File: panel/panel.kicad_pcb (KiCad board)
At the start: 0 parts

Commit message: LED matrix placement
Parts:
- added C1: 0.1uF, Capacitor_SMD:C_0603_1608Metric, F.Cu at (322.1, 98.3)
- added C2: 0.1uF, Capacitor_SMD:C_0603_1608Metric, F.Cu at (338.8, 87.2)
- added C3: 0.1uF, Capacitor_SMD:C_0603_1608Metric, F.Cu at (330.9, 93.8)
- added C4: 0.1uF, Capacitor_SMD:C_0603_1608Metric, F.Cu at (326.1, 98.3)
- added D1: LED_RABG, panel:MHPA1515RGBDT, F.Cu at (61.5, 61.5)
- added D10: LED_RABG, panel:MHPA1515RGBDT, F.Cu at (81.3, 61.5)
- added D100: LED_RABG, panel:MHPA1515RGBDT, F.Cu at (68.1, 74.7)
- added D101: LED_RABG, panel:MHPA1515RGBDT, F.Cu at (70.3, 74.7)
- added D102: LED_RABG, panel:MHPA1515RGBDT, F.Cu at (72.5, 74.7)
- added D103: LED_RABG, panel:MHPA1515RGBDT, F.Cu at (74.7, 74.7)
- added D104: LED_RABG, panel:MHPA1515RGBDT, F.Cu at (76.9, 74.7)
- added D105: LED_RABG, panel:MHPA1515RGBDT, F.Cu at (79.1, 74.7)
- added D106: LED_RABG, panel:MHPA1515RGBDT, F.Cu at (81.3, 74.7)
- added D107: LED_RABG, panel:MHPA1515RGBDT, F.Cu at (83.5, 74.7)
- added D108: LED_RABG, panel:MHPA1515RGBDT, F.Cu at (85.7, 74.7)
- added D109: LED_RABG, panel:MHPA1515RGBDT, F.Cu at (87.9, 74.7)
- added D11: LED_RABG, panel:MHPA1515RGBDT, F.Cu at (83.5, 61.5)
- added D110: LED_RABG, panel:MHPA1515RGBDT, F.Cu at (90.1, 74.7)
- added D111: LED_RABG, panel:MHPA1515RGBDT, F.Cu at (92.3, 74.7)
- added D112: LED_RABG, panel:MHPA1515RGBDT, F.Cu at (94.5, 74.7)
- added D113: LED_RABG, panel:MHPA1515RGBDT, F.Cu at (61.5, 76.9)
- added D114: LED_RABG, panel:MHPA1515RGBDT, F.Cu at (63.7, 76.9)
- added D115: LED_RABG, panel:MHPA1515RGBDT, F.Cu at (65.9, 76.9)
- added D116: LED_RABG, panel:MHPA1515RGBDT, F.Cu at (68.1, 76.9)
- added D117: LED_RABG, panel:MHPA1515RGBDT, F.Cu at (70.3, 76.9)
- added D118: LED_RABG, panel:MHPA1515RGBDT, F.Cu at (72.5, 76.9)
- added D119: LED_RABG, panel:MHPA1515RGBDT, F.Cu at (74.7, 76.9)
- added D12: LED_RABG, panel:MHPA1515RGBDT, F.Cu at (85.7, 61.5)
- added D120: LED_RABG, panel:MHPA1515RGBDT, F.Cu at (76.9, 76.9)
- added D121: LED_RABG, panel:MHPA1515RGBDT, F.Cu at (79.1, 76.9)
- added D122: LED_RABG, panel:MHPA1515RGBDT, F.Cu at (81.3, 76.9)
- added D123: LED_RABG, panel:MHPA1515RGBDT, F.Cu at (83.5, 76.9)
- added D124: LED_RABG, panel:MHPA1515RGBDT, F.Cu at (85.7, 76.9)
- added D125: LED_RABG, panel:MHPA1515RGBDT, F.Cu at (87.9, 76.9)
- added D126: LED_RABG, panel:MHPA1515RGBDT, F.Cu at (90.1, 76.9)
- added D127: LED_RABG, panel:MHPA1515RGBDT, F.Cu at (92.3, 76.9)
- added D128: LED_RABG, panel:MHPA1515RGBDT, F.Cu at (94.5, 76.9)
- added D129: LED_RABG, panel:MHPA1515RGBDT, F.Cu at (61.5, 79.1)
- added D13: LED_RABG, panel:MHPA1515RGBDT, F.Cu at (87.9, 61.5)
- added D130: LED_RABG, panel:MHPA1515RGBDT, F.Cu at (63.7, 79.1)
- added D131: LED_RABG, panel:MHPA1515RGBDT, F.Cu at (65.9, 79.1)
- added D132: LED_RABG, panel:MHPA1515RGBDT, F.Cu at (68.1, 79.1)
- added D133: LED_RABG, panel:MHPA1515RGBDT, F.Cu at (70.3, 79.1)
- added D134: LED_RABG, panel:MHPA1515RGBDT, F.Cu at (72.5, 79.1)
- added D135: LED_RABG, panel:MHPA1515RGBDT, F.Cu at (74.7, 79.1)
- added D136: LED_RABG, panel:MHPA1515RGBDT, F.Cu at (76.9, 79.1)
- added D137: LED_RABG, panel:MHPA1515RGBDT, F.Cu at (79.1, 79.1)
- added D138: LED_RABG, panel:MHPA1515RGBDT, F.Cu at (81.3, 79.1)
- added D139: LED_RABG, panel:MHPA1515RGBDT, F.Cu at (83.5, 79.1)
- added D14: LED_RABG, panel:MHPA1515RGBDT, F.Cu at (90.1, 61.5)
- added D140: LED_RABG, panel:MHPA1515RGBDT, F.Cu at (85.7, 79.1)
- added D141: LED_RABG, panel:MHPA1515RGBDT, F.Cu at (87.9, 79.1)
- added D142: LED_RABG, panel:MHPA1515RGBDT, F.Cu at (90.1, 79.1)
- added D143: LED_RABG, panel:MHPA1515RGBDT, F.Cu at (92.3, 79.1)
- added D144: LED_RABG, panel:MHPA1515RGBDT, F.Cu at (94.5, 79.1)
- added D145: LED_RABG, panel:MHPA1515RGBDT, F.Cu at (61.5, 81.3)
- added D146: LED_RABG, panel:MHPA1515RGBDT, F.Cu at (63.7, 81.3)
- added D147: LED_RABG, panel:MHPA1515RGBDT, F.Cu at (65.9, 81.3)
- added D148: LED_RABG, panel:MHPA1515RGBDT, F.Cu at (68.1, 81.3)
- added D149: LED_RABG, panel:MHPA1515RGBDT, F.Cu at (70.3, 81.3)
- added D15: LED_RABG, panel:MHPA1515RGBDT, F.Cu at (92.3, 61.5)
- added D150: LED_RABG, panel:MHPA1515RGBDT, F.Cu at (72.5, 81.3)
- added D151: LED_RABG, panel:MHPA1515RGBDT, F.Cu at (74.7, 81.3)
- added D152: LED_RABG, panel:MHPA1515RGBDT, F.Cu at (76.9, 81.3)
- added D153: LED_RABG, panel:MHPA1515RGBDT, F.Cu at (79.1, 81.3)
- added D154: LED_RABG, panel:MHPA1515RGBDT, F.Cu at (81.3, 81.3)
- added D155: LED_RABG, panel:MHPA1515RGBDT, F.Cu at (83.5, 81.3)
- added D156: LED_RABG, panel:MHPA1515RGBDT, F.Cu at (85.7, 81.3)
- added D157: LED_RABG, panel:MHPA1515RGBDT, F.Cu at (87.9, 81.3)
- added D158: LED_RABG, panel:MHPA1515RGBDT, F.Cu at (90.1, 81.3)
- added D159: LED_RABG, panel:MHPA1515RGBDT, F.Cu at (92.3, 81.3)
- added D16: LED_RABG, panel:MHPA1515RGBDT, F.Cu at (94.5, 61.5)
- added D160: LED_RABG, panel:MHPA1515RGBDT, F.Cu at (94.5, 81.3)
- added D161: LED_RABG, panel:MHPA1515RGBDT, F.Cu at (61.5, 83.5)
- added D162: LED_RABG, panel:MHPA1515RGBDT, F.Cu at (63.7, 83.5)
- added D163: LED_RABG, panel:MHPA1515RGBDT, F.Cu at (65.9, 83.5)
- added D164: LED_RABG, panel:MHPA1515RGBDT, F.Cu at (68.1, 83.5)
- added D165: LED_RABG, panel:MHPA1515RGBDT, F.Cu at (70.3, 83.5)
- added D166: LED_RABG, panel:MHPA1515RGBDT, F.Cu at (72.5, 83.5)
- added D167: LED_RABG, panel:MHPA1515RGBDT, F.Cu at (74.7, 83.5)
- added D168: LED_RABG, panel:MHPA1515RGBDT, F.Cu at (76.9, 83.5)
- added D169: LED_RABG, panel:MHPA1515RGBDT, F.Cu at (79.1, 83.5)
- added D17: LED_RABG, panel:MHPA1515RGBDT, F.Cu at (61.5, 63.7)
- added D170: LED_RABG, panel:MHPA1515RGBDT, F.Cu at (81.3, 83.5)
- added D171: LED_RABG, panel:MHPA1515RGBDT, F.Cu at (83.5, 83.5)
- added D172: LED_RABG, panel:MHPA1515RGBDT, F.Cu at (85.7, 83.5)
- added D173: LED_RABG, panel:MHPA1515RGBDT, F.Cu at (87.9, 83.5)
- added D174: LED_RABG, panel:MHPA1515RGBDT, F.Cu at (90.1, 83.5)
- added D175: LED_RABG, panel:MHPA1515RGBDT, F.Cu at (92.3, 83.5)
- added D176: LED_RABG, panel:MHPA1515RGBDT, F.Cu at (94.5, 83.5)
- added D177: LED_RABG, panel:MHPA1515RGBDT, F.Cu at (61.5, 85.7)
- added D178: LED_RABG, panel:MHPA1515RGBDT, F.Cu at (63.7, 85.7)
- added D179: LED_RABG, panel:MHPA1515RGBDT, F.Cu at (65.9, 85.7)
- added D18: LED_RABG, panel:MHPA1515RGBDT, F.Cu at (63.7, 63.7)
- added D180: LED_RABG, panel:MHPA1515RGBDT, F.Cu at (68.1, 85.7)
- added D181: LED_RABG, panel:MHPA1515RGBDT, F.Cu at (70.3, 85.7)
- added D182: LED_RABG, panel:MHPA1515RGBDT, F.Cu at (72.5, 85.7)
- added D183: LED_RABG, panel:MHPA1515RGBDT, F.Cu at (74.7, 85.7)
- added D184: LED_RABG, panel:MHPA1515RGBDT, F.Cu at (76.9, 85.7)
- added D185: LED_RABG, panel:MHPA1515RGBDT, F.Cu at (79.1, 85.7)
- added D186: LED_RABG, panel:MHPA1515RGBDT, F.Cu at (81.3, 85.7)
- added D187: LED_RABG, panel:MHPA1515RGBDT, F.Cu at (83.5, 85.7)
- added D188: LED_RABG, panel:MHPA1515RGBDT, F.Cu at (85.7, 85.7)
- added D189: LED_RABG, panel:MHPA1515RGBDT, F.Cu at (87.9, 85.7)
- added D19: LED_RABG, panel:MHPA1515RGBDT, F.Cu at (65.9, 63.7)
- added D190: LED_RABG, panel:MHPA1515RGBDT, F.Cu at (90.1, 85.7)
- added D191: LED_RABG, panel:MHPA1515RGBDT, F.Cu at (92.3, 85.7)
- added D192: LED_RABG, panel:MHPA1515RGBDT, F.Cu at (94.5, 85.7)
- added D193: LED_RABG, panel:MHPA1515RGBDT, F.Cu at (61.5, 87.9)
- added D194: LED_RABG, panel:MHPA1515RGBDT, F.Cu at (63.7, 87.9)
- added D195: LED_RABG, panel:MHPA1515RGBDT, F.Cu at (65.9, 87.9)
- added D196: LED_RABG, panel:MHPA1515RGBDT, F.Cu at (68.1, 87.9)
- added D197: LED_RABG, panel:MHPA1515RGBDT, F.Cu at (70.3, 87.9)
- added D198: LED_RABG, panel:MHPA1515RGBDT, F.Cu at (72.5, 87.9)
- added D199: LED_RABG, panel:MHPA1515RGBDT, F.Cu at (74.7, 87.9)
- added D2: LED_RABG, panel:MHPA1515RGBDT, F.Cu at (63.7, 61.5)
- added D20: LED_RABG, panel:MHPA1515RGBDT, F.Cu at (68.1, 63.7)
- added D200: LED_RABG, panel:MHPA1515RGBDT, F.Cu at (76.9, 87.9)
- added D201: LED_RABG, panel:MHPA1515RGBDT, F.Cu at (79.1, 87.9)
- added D202: LED_RABG, panel:MHPA1515RGBDT, F.Cu at (81.3, 87.9)
- added D203: LED_RABG, panel:MHPA1515RGBDT, F.Cu at (83.5, 87.9)
- added D204: LED_RABG, panel:MHPA1515RGBDT, F.Cu at (85.7, 87.9)
- added D205: LED_RABG, panel:MHPA1515RGBDT, F.Cu at (87.9, 87.9)
- added D206: LED_RABG, panel:MHPA1515RGBDT, F.Cu at (90.1, 87.9)
- added D207: LED_RABG, panel:MHPA1515RGBDT, F.Cu at (92.3, 87.9)
- added D208: LED_RABG, panel:MHPA1515RGBDT, F.Cu at (94.5, 87.9)
- added D209: LED_RABG, panel:MHPA1515RGBDT, F.Cu at (61.5, 90.1)
- added D21: LED_RABG, panel:MHPA1515RGBDT, F.Cu at (70.3, 63.7)
- added D210: LED_RABG, panel:MHPA1515RGBDT, F.Cu at (63.7, 90.1)
- added D211: LED_RABG, panel:MHPA1515RGBDT, F.Cu at (65.9, 90.1)
- added D212: LED_RABG, panel:MHPA1515RGBDT, F.Cu at (68.1, 90.1)
- added D213: LED_RABG, panel:MHPA1515RGBDT, F.Cu at (70.3, 90.1)
- added D214: LED_RABG, panel:MHPA1515RGBDT, F.Cu at (72.5, 90.1)
- added D215: LED_RABG, panel:MHPA1515RGBDT, F.Cu at (74.7, 90.1)
- added D216: LED_RABG, panel:MHPA1515RGBDT, F.Cu at (76.9, 90.1)
- added D217: LED_RABG, panel:MHPA1515RGBDT, F.Cu at (79.1, 90.1)
- added D218: LED_RABG, panel:MHPA1515RGBDT, F.Cu at (81.3, 90.1)
- added D219: LED_RABG, panel:MHPA1515RGBDT, F.Cu at (83.5, 90.1)
- added D22: LED_RABG, panel:MHPA1515RGBDT, F.Cu at (72.5, 63.7)
- added D220: LED_RABG, panel:MHPA1515RGBDT, F.Cu at (85.7, 90.1)
- added D221: LED_RABG, panel:MHPA1515RGBDT, F.Cu at (87.9, 90.1)
- added D222: LED_RABG, panel:MHPA1515RGBDT, F.Cu at (90.1, 90.1)
- added D223: LED_RABG, panel:MHPA1515RGBDT, F.Cu at (92.3, 90.1)
- added D224: LED_RABG, panel:MHPA1515RGBDT, F.Cu at (94.5, 90.1)
- added D225: LED_RABG, panel:MHPA1515RGBDT, F.Cu at (61.5, 92.3)
- added D226: LED_RABG, panel:MHPA1515RGBDT, F.Cu at (63.7, 92.3)
- added D227: LED_RABG, panel:MHPA1515RGBDT, F.Cu at (65.9, 92.3)
- added D228: LED_RABG, panel:MHPA1515RGBDT, F.Cu at (68.1, 92.3)
- added D229: LED_RABG, panel:MHPA1515RGBDT, F.Cu at (70.3, 92.3)
- added D23: LED_RABG, panel:MHPA1515RGBDT, F.Cu at (74.7, 63.7)
- added D230: LED_RABG, panel:MHPA1515RGBDT, F.Cu at (72.5, 92.3)
- added D231: LED_RABG, panel:MHPA1515RGBDT, F.Cu at (74.7, 92.3)
- added D232: LED_RABG, panel:MHPA1515RGBDT, F.Cu at (76.9, 92.3)
- added D233: LED_RABG, panel:MHPA1515RGBDT, F.Cu at (79.1, 92.3)
- added D234: LED_RABG, panel:MHPA1515RGBDT, F.Cu at (81.3, 92.3)
- added D235: LED_RABG, panel:MHPA1515RGBDT, F.Cu at (83.5, 92.3)
- added D236: LED_RABG, panel:MHPA1515RGBDT, F.Cu at (85.7, 92.3)
- added D237: LED_RABG, panel:MHPA1515RGBDT, F.Cu at (87.9, 92.3)
- added D238: LED_RABG, panel:MHPA1515RGBDT, F.Cu at (90.1, 92.3)
- added D239: LED_RABG, panel:MHPA1515RGBDT, F.Cu at (92.3, 92.3)
- added D24: LED_RABG, panel:MHPA1515RGBDT, F.Cu at (76.9, 63.7)
- added D240: LED_RABG, panel:MHPA1515RGBDT, F.Cu at (94.5, 92.3)
- added D241: LED_RABG, panel:MHPA1515RGBDT, F.Cu at (61.5, 94.5)
- added D242: LED_RABG, panel:MHPA1515RGBDT, F.Cu at (63.7, 94.5)
- added D243: LED_RABG, panel:MHPA1515RGBDT, F.Cu at (65.9, 94.5)
- added D244: LED_RABG, panel:MHPA1515RGBDT, F.Cu at (68.1, 94.5)
- added D245: LED_RABG, panel:MHPA1515RGBDT, F.Cu at (70.3, 94.5)
- added D246: LED_RABG, panel:MHPA1515RGBDT, F.Cu at (72.5, 94.5)
- added D247: LED_RABG, panel:MHPA1515RGBDT, F.Cu at (74.7, 94.5)
- added D248: LED_RABG, panel:MHPA1515RGBDT, F.Cu at (76.9, 94.5)
- added D249: LED_RABG, panel:MHPA1515RGBDT, F.Cu at (79.1, 94.5)
- added D25: LED_RABG, panel:MHPA1515RGBDT, F.Cu at (79.1, 63.7)
- added D250: LED_RABG, panel:MHPA1515RGBDT, F.Cu at (81.3, 94.5)
- added D251: LED_RABG, panel:MHPA1515RGBDT, F.Cu at (83.5, 94.5)
- added D252: LED_RABG, panel:MHPA1515RGBDT, F.Cu at (85.7, 94.5)
- added D253: LED_RABG, panel:MHPA1515RGBDT, F.Cu at (87.9, 94.5)
- added D254: LED_RABG, panel:MHPA1515RGBDT, F.Cu at (90.1, 94.5)
- added D255: LED_RABG, panel:MHPA1515RGBDT, F.Cu at (92.3, 94.5)
- added D256: LED_RABG, panel:MHPA1515RGBDT, F.Cu at (94.5, 94.5)
- added D26: LED_RABG, panel:MHPA1515RGBDT, F.Cu at (81.3, 63.7)
- added D27: LED_RABG, panel:MHPA1515RGBDT, F.Cu at (83.5, 63.7)
- added D28: LED_RABG, panel:MHPA1515RGBDT, F.Cu at (85.7, 63.7)
- added D29: LED_RABG, panel:MHPA1515RGBDT, F.Cu at (87.9, 63.7)
- added D3: LED_RABG, panel:MHPA1515RGBDT, F.Cu at (65.9, 61.5)
- added D30: LED_RABG, panel:MHPA1515RGBDT, F.Cu at (90.1, 63.7)
- added D31: LED_RABG, panel:MHPA1515RGBDT, F.Cu at (92.3, 63.7)
- added D32: LED_RABG, panel:MHPA1515RGBDT, F.Cu at (94.5, 63.7)
- added D33: LED_RABG, panel:MHPA1515RGBDT, F.Cu at (61.5, 65.9)
- added D34: LED_RABG, panel:MHPA1515RGBDT, F.Cu at (63.7, 65.9)
- added D35: LED_RABG, panel:MHPA1515RGBDT, F.Cu at (65.9, 65.9)
- added D36: LED_RABG, panel:MHPA1515RGBDT, F.Cu at (68.1, 65.9)
- added D37: LED_RABG, panel:MHPA1515RGBDT, F.Cu at (70.3, 65.9)
- added D38: LED_RABG, panel:MHPA1515RGBDT, F.Cu at (72.5, 65.9)
- added D39: LED_RABG, panel:MHPA1515RGBDT, F.Cu at (74.7, 65.9)
- added D4: LED_RABG, panel:MHPA1515RGBDT, F.Cu at (68.1, 61.5)
- added D40: LED_RABG, panel:MHPA1515RGBDT, F.Cu at (76.9, 65.9)
- added D41: LED_RABG, panel:MHPA1515RGBDT, F.Cu at (79.1, 65.9)
- added D42: LED_RABG, panel:MHPA1515RGBDT, F.Cu at (81.3, 65.9)
- added D43: LED_RABG, panel:MHPA1515RGBDT, F.Cu at (83.5, 65.9)
- added D44: LED_RABG, panel:MHPA1515RGBDT, F.Cu at (85.7, 65.9)
- added D45: LED_RABG, panel:MHPA1515RGBDT, F.Cu at (87.9, 65.9)
- added D46: LED_RABG, panel:MHPA1515RGBDT, F.Cu at (90.1, 65.9)
- added D47: LED_RABG, panel:MHPA1515RGBDT, F.Cu at (92.3, 65.9)
- added D48: LED_RABG, panel:MHPA1515RGBDT, F.Cu at (94.5, 65.9)
- added D49: LED_RABG, panel:MHPA1515RGBDT, F.Cu at (61.5, 68.1)
- added D5: LED_RABG, panel:MHPA1515RGBDT, F.Cu at (70.3, 61.5)
- added D50: LED_RABG, panel:MHPA1515RGBDT, F.Cu at (63.7, 68.1)
- added D51: LED_RABG, panel:MHPA1515RGBDT, F.Cu at (65.9, 68.1)
- added D52: LED_RABG, panel:MHPA1515RGBDT, F.Cu at (68.1, 68.1)
- added D53: LED_RABG, panel:MHPA1515RGBDT, F.Cu at (70.3, 68.1)
- added D54: LED_RABG, panel:MHPA1515RGBDT, F.Cu at (72.5, 68.1)
- added D55: LED_RABG, panel:MHPA1515RGBDT, F.Cu at (74.7, 68.1)
- added D56: LED_RABG, panel:MHPA1515RGBDT, F.Cu at (76.9, 68.1)
- added D57: LED_RABG, panel:MHPA1515RGBDT, F.Cu at (79.1, 68.1)
- added D58: LED_RABG, panel:MHPA1515RGBDT, F.Cu at (81.3, 68.1)
- added D59: LED_RABG, panel:MHPA1515RGBDT, F.Cu at (83.5, 68.1)
- added D6: LED_RABG, panel:MHPA1515RGBDT, F.Cu at (72.5, 61.5)
- added D60: LED_RABG, panel:MHPA1515RGBDT, F.Cu at (85.7, 68.1)
- added D61: LED_RABG, panel:MHPA1515RGBDT, F.Cu at (87.9, 68.1)
- added D62: LED_RABG, panel:MHPA1515RGBDT, F.Cu at (90.1, 68.1)
- added D63: LED_RABG, panel:MHPA1515RGBDT, F.Cu at (92.3, 68.1)
- added D64: LED_RABG, panel:MHPA1515RGBDT, F.Cu at (94.5, 68.1)
- added D65: LED_RABG, panel:MHPA1515RGBDT, F.Cu at (61.5, 70.3)
- added D66: LED_RABG, panel:MHPA1515RGBDT, F.Cu at (63.7, 70.3)
- added D67: LED_RABG, panel:MHPA1515RGBDT, F.Cu at (65.9, 70.3)
- added D68: LED_RABG, panel:MHPA1515RGBDT, F.Cu at (68.1, 70.3)
- added D69: LED_RABG, panel:MHPA1515RGBDT, F.Cu at (70.3, 70.3)
- added D7: LED_RABG, panel:MHPA1515RGBDT, F.Cu at (74.7, 61.5)
- added D70: LED_RABG, panel:MHPA1515RGBDT, F.Cu at (72.5, 70.3)
- added D71: LED_RABG, panel:MHPA1515RGBDT, F.Cu at (74.7, 70.3)
- added D72: LED_RABG, panel:MHPA1515RGBDT, F.Cu at (76.9, 70.3)
- added D73: LED_RABG, panel:MHPA1515RGBDT, F.Cu at (79.1, 70.3)
- added D74: LED_RABG, panel:MHPA1515RGBDT, F.Cu at (81.3, 70.3)
- added D75: LED_RABG, panel:MHPA1515RGBDT, F.Cu at (83.5, 70.3)
- added D76: LED_RABG, panel:MHPA1515RGBDT, F.Cu at (85.7, 70.3)
- added D77: LED_RABG, panel:MHPA1515RGBDT, F.Cu at (87.9, 70.3)
- added D78: LED_RABG, panel:MHPA1515RGBDT, F.Cu at (90.1, 70.3)
- added D79: LED_RABG, panel:MHPA1515RGBDT, F.Cu at (92.3, 70.3)
- added D8: LED_RABG, panel:MHPA1515RGBDT, F.Cu at (76.9, 61.5)
- added D80: LED_RABG, panel:MHPA1515RGBDT, F.Cu at (94.5, 70.3)
- added D81: LED_RABG, panel:MHPA1515RGBDT, F.Cu at (61.5, 72.5)
- added D82: LED_RABG, panel:MHPA1515RGBDT, F.Cu at (63.7, 72.5)
- added D83: LED_RABG, panel:MHPA1515RGBDT, F.Cu at (65.9, 72.5)
- added D84: LED_RABG, panel:MHPA1515RGBDT, F.Cu at (68.1, 72.5)
- added D85: LED_RABG, panel:MHPA1515RGBDT, F.Cu at (70.3, 72.5)
- added D86: LED_RABG, panel:MHPA1515RGBDT, F.Cu at (72.5, 72.5)
- added D87: LED_RABG, panel:MHPA1515RGBDT, F.Cu at (74.7, 72.5)
- added D88: LED_RABG, panel:MHPA1515RGBDT, F.Cu at (76.9, 72.5)
- added D89: LED_RABG, panel:MHPA1515RGBDT, F.Cu at (79.1, 72.5)
- added D9: LED_RABG, panel:MHPA1515RGBDT, F.Cu at (79.1, 61.5)
- added D90: LED_RABG, panel:MHPA1515RGBDT, F.Cu at (81.3, 72.5)
- added D91: LED_RABG, panel:MHPA1515RGBDT, F.Cu at (83.5, 72.5)
- added D92: LED_RABG, panel:MHPA1515RGBDT, F.Cu at (85.7, 72.5)
- added D93: LED_RABG, panel:MHPA1515RGBDT, F.Cu at (87.9, 72.5)
- added D94: LED_RABG, panel:MHPA1515RGBDT, F.Cu at (90.1, 72.5)
- added D95: LED_RABG, panel:MHPA1515RGBDT, F.Cu at (92.3, 72.5)
- added D96: LED_RABG, panel:MHPA1515RGBDT, F.Cu at (94.5, 72.5)
- added D97: LED_RABG, panel:MHPA1515RGBDT, F.Cu at (61.5, 74.7)
- added D98: LED_RABG, panel:MHPA1515RGBDT, F.Cu at (63.7, 74.7)
- added D99: LED_RABG, panel:MHPA1515RGBDT, F.Cu at (65.9, 74.7)
- added J1: IN, panel:5034800600, F.Cu at (332.0, 89.8)
- added J2: OUT, panel:5034800600, F.Cu at (339.9, 83.3)
- added Q1: Q_PMOS_GSD, Package_TO_SOT_SMD:SOT-883, F.Cu at (335.4, 96.8)
- added Q10: Q_PMOS_GSD, Package_TO_SOT_SMD:SOT-883, F.Cu at (328.1, 100.7)
- added Q11: Q_PMOS_GSD, Package_TO_SOT_SMD:SOT-883, F.Cu at (344.4, 83.8)
- added Q12: Q_PMOS_GSD, Package_TO_SOT_SMD:SOT-883, F.Cu at (344.8, 86.1)
- added Q13: Q_PMOS_GSD, Package_TO_SOT_SMD:SOT-883, F.Cu at (343.1, 89.4)
- added Q14: Q_PMOS_GSD, Package_TO_SOT_SMD:SOT-883, F.Cu at (336.5, 92.1)
- added Q15: Q_PMOS_GSD, Package_TO_SOT_SMD:SOT-883, F.Cu at (339.1, 92.1)
- added Q16: Q_PMOS_GSD, Package_TO_SOT_SMD:SOT-883, F.Cu at (332.8, 96.2)
- added Q2: Q_PMOS_GSD, Package_TO_SOT_SMD:SOT-883, F.Cu at (332.8, 98.5)
- added Q3: Q_PMOS_GSD, Package_TO_SOT_SMD:SOT-883, F.Cu at (349.6, 83.6)
- added Q4: Q_PMOS_GSD, Package_TO_SOT_SMD:SOT-883, F.Cu at (348.4, 81.3)
- added Q5: Q_PMOS_GSD, Package_TO_SOT_SMD:SOT-883, F.Cu at (340.5, 89.6)
- added Q6: Q_PMOS_GSD, Package_TO_SOT_SMD:SOT-883, F.Cu at (342.2, 87.1)
- added Q7: Q_PMOS_GSD, Package_TO_SOT_SMD:SOT-883, F.Cu at (338.0, 94.5)
- added Q8: Q_PMOS_GSD, Package_TO_SOT_SMD:SOT-883, F.Cu at (347.0, 83.8)
- added Q9: Q_PMOS_GSD, Package_TO_SOT_SMD:SOT-883, F.Cu at (335.4, 94.5)
- added R1: 2.2k, Resistor_SMD:R_0603_1608Metric, F.Cu at (345.1, 81.4)
- added R2: 7.5k, Resistor_SMD:R_0603_1608Metric, F.Cu at (337.1, 89.7)
- added R3: 4.12k, Resistor_SMD:R_0603_1608Metric, F.Cu at (322.1, 100.8)
- added U1: TLC59025, Package_SO:SSOP-24_3.9x8.7mm_P0.635mm, F.Cu at (316.1, 85.3)
- added U2: TLC59025, Package_SO:SSOP-24_3.9x8.7mm_P0.635mm, F.Cu at (324.1, 85.3)
- added U3: TLC59025, Package_SO:SSOP-24_3.9x8.7mm_P0.635mm, F.Cu at (316.1, 95.6)
- added U4: SN74HC595, Package_SO:TSSOP-16_4.4x5mm_P0.65mm, F.Cu at (324.5, 93.8)
- added U5: SN74HC595, Package_SO:TSSOP-16_4.4x5mm_P0.65mm, F.Cu at (332.4, 83.4)
- added U6: NC7WZ17, Package_SON:Fairchild_MicroPak2-6_1.0x1.0mm_P0.35mm, F.Cu at (330.2, 96.2)
- added U7: NC7WZ17, Package_SON:Fairchild_MicroPak2-6_1.0x1.0mm_P0.35mm, F.Cu at (325.4, 100.8)
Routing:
- net /ROW_0/COMMON: track 0.00 -> 8.00 mm, vias 0 -> 16
- net COL_9B: track 0.00 -> 2.92 mm
- net COL_5B: track 0.00 -> 2.92 mm
- net COL_4B: track 0.00 -> 2.92 mm
- net COL_15B: track 0.00 -> 2.92 mm
- net COL_14B: track 0.00 -> 2.92 mm
- net COL_10B: track 0.00 -> 2.92 mm
- net COL_1B: track 0.00 -> 2.92 mm
- net COL_7B: track 0.00 -> 2.92 mm
- net COL_13B: track 0.00 -> 2.92 mm
- net COL_8B: track 0.00 -> 2.92 mm
- net COL_3B: track 0.00 -> 2.92 mm
- net COL_2B: track 0.00 -> 2.92 mm
- net COL_12B: track 0.00 -> 2.92 mm
- net COL_0B: track 0.00 -> 2.92 mm
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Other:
- board outline added: 36 x 36 mm
- copper layers 0 -> 4

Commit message: Routed columns
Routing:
- net COL_9B: track 2.92 -> 44.0 mm
- net COL_15B: track 2.92 -> 44.0 mm
- net COL_5B: track 2.92 -> 44.0 mm
- net COL_14B: track 2.92 -> 44.0 mm
- net COL_10B: track 2.92 -> 44.0 mm
- net COL_4B: track 2.92 -> 44.0 mm
- net COL_1B: track 2.92 -> 44.0 mm
- net COL_2B: track 2.92 -> 44.0 mm
- net COL_8B: track 2.92 -> 44.0 mm
- net COL_7B: track 2.92 -> 44.0 mm
- net COL_3B: track 2.92 -> 44.0 mm
- net COL_13B: track 2.92 -> 44.0 mm
- net COL_12B: track 2.92 -> 44.0 mm
- net COL_0B: track 2.92 -> 44.0 mm
- net COL_6B: track 2.92 -> 44.0 mm
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
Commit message: Routed rows
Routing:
- net /ROW_2/COMMON: track 8.00 -> 49.4 mm
- net /ROW_13/COMMON: track 8.00 -> 49.4 mm
- net /ROW_8/COMMON: track 8.00 -> 49.4 mm
- net /ROW_7/COMMON: track 8.00 -> 49.4 mm
- net /ROW_1/COMMON: track 8.00 -> 49.4 mm
- net /ROW_6/COMMON: track 8.00 -> 49.4 mm
- net /ROW_3/COMMON: track 8.00 -> 49.4 mm
- net /ROW_12/COMMON: track 8.00 -> 49.4 mm
- net /ROW_11/COMMON: track 8.00 -> 49.4 mm
- net /ROW_0/COMMON: track 8.00 -> 49.4 mm
- net /ROW_9/COMMON: track 8.00 -> 49.4 mm
- net /ROW_4/COMMON: track 8.00 -> 49.4 mm
- net /ROW_14/COMMON: track 8.00 -> 49.4 mm
- net /ROW_5/COMMON: track 8.00 -> 49.4 mm
- net /ROW_10/COMMON: track 8.00 -> 49.4 mm
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
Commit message: Modified column routing
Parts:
- moved C1 193.1 mm to (130.3, 121.4)
- moved C3 193.1 mm to (139.1, 116.9)
- moved J1 193.1 mm to (140.2, 113.0)
- moved J2 193.1 mm to (148.2, 106.4)
- moved Q10 193.1 mm to (136.4, 123.9)
- moved Q11 193.1 mm to (152.7, 106.9)
- moved Q16 193.1 mm to (141.1, 119.3)
- moved Q2 193.1 mm to (141.1, 121.7)
- moved Q3 193.1 mm to (157.8, 106.8)
- moved Q5 193.1 mm to (148.7, 112.7)
- moved R2 193.1 mm to (145.3, 112.8)
- moved R3 193.1 mm to (130.3, 124.0)
- moved U4 193.1 mm to (132.7, 116.9)
- moved U5 193.1 mm to (140.7, 106.5)
- moved U6 193.1 mm to (138.4, 119.4)
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
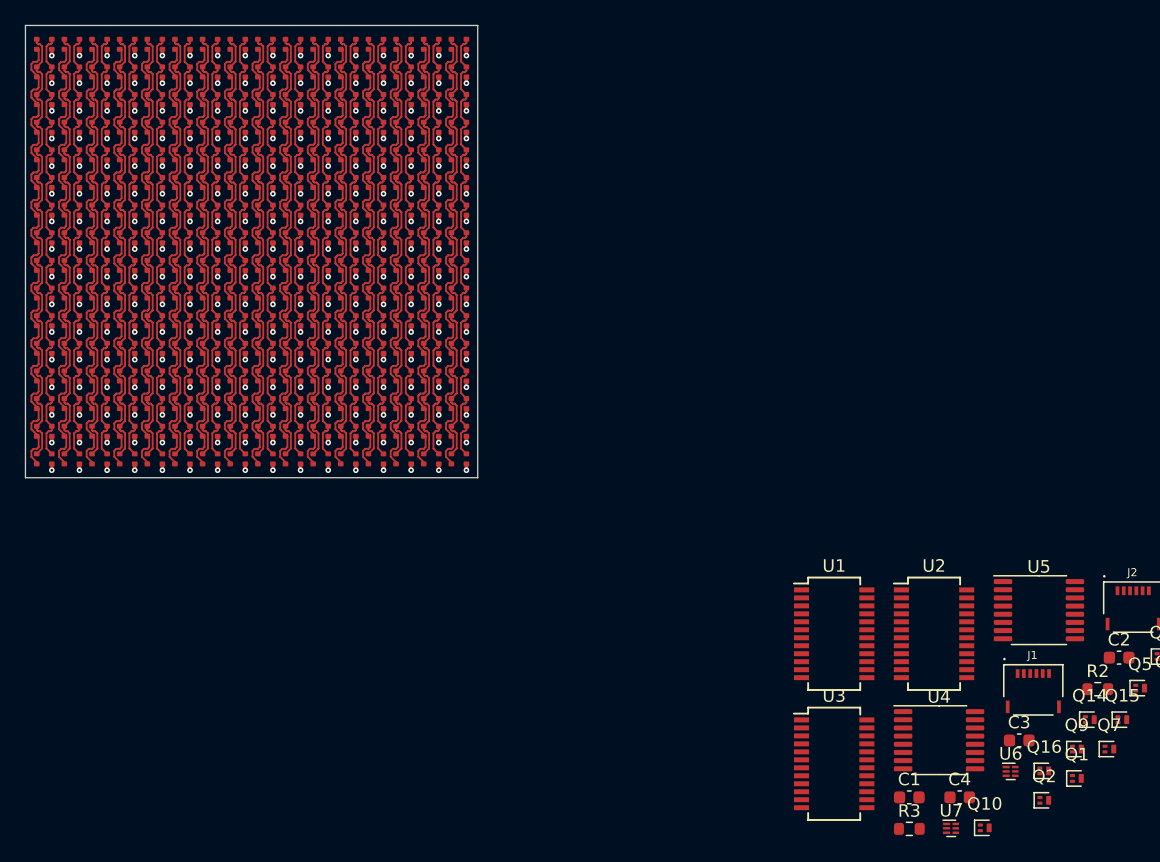
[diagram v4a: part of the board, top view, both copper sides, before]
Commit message: Routing fixes and CC drivers placed
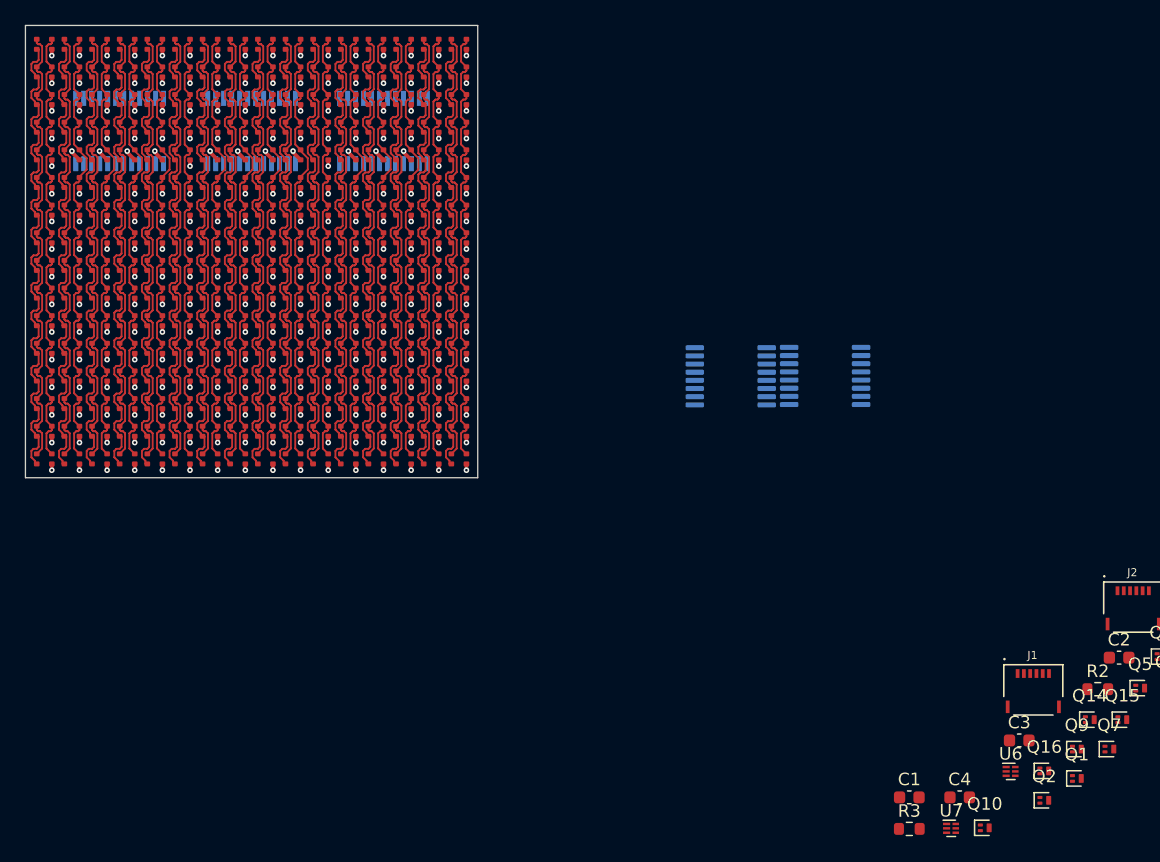
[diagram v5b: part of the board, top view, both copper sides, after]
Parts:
- U1, U2, U3, U4, U5: moved to B.Cu
- moved U3 76.0 mm to (67.5, 68.4), turned to -90 degrees
- moved U2 67.5 mm to (78.0, 68.4), turned to -90 degrees
- moved U1 53.7 mm to (88.5, 68.4), turned to -90 degrees
- moved U4 33.4 mm to (116.1, 87.9), turned to 180 degrees
- moved U5 25.2 mm to (123.7, 87.9), turned to 180 degrees
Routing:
- net COL_13B: track 43.9 -> 45.1 mm
- net COL_8B: track 43.9 -> 45.1 mm
- net COL_3B: track 43.9 -> 45.1 mm
- net COL_9B: track 43.9 -> 45.1 mm
- net COL_14B: track 43.9 -> 45.1 mm
- net COL_5B: track 43.9 -> 45.1 mm
- net COL_1B: track 43.9 -> 45.1 mm
- net COL_10B: track 43.9 -> 45.1 mm
- net COL_7B: track 43.9 -> 45.1 mm
- net COL_4B: track 43.9 -> 45.1 mm
- net COL_2B: track 43.9 -> 45.1 mm
- net COL_15B: track 43.9 -> 45.1 mm
- net COL_12B: track 43.9 -> 45.1 mm
- net COL_0B: track 43.9 -> 45.1 mm
- net COL_11B: track 43.9 -> 45.1 mm
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
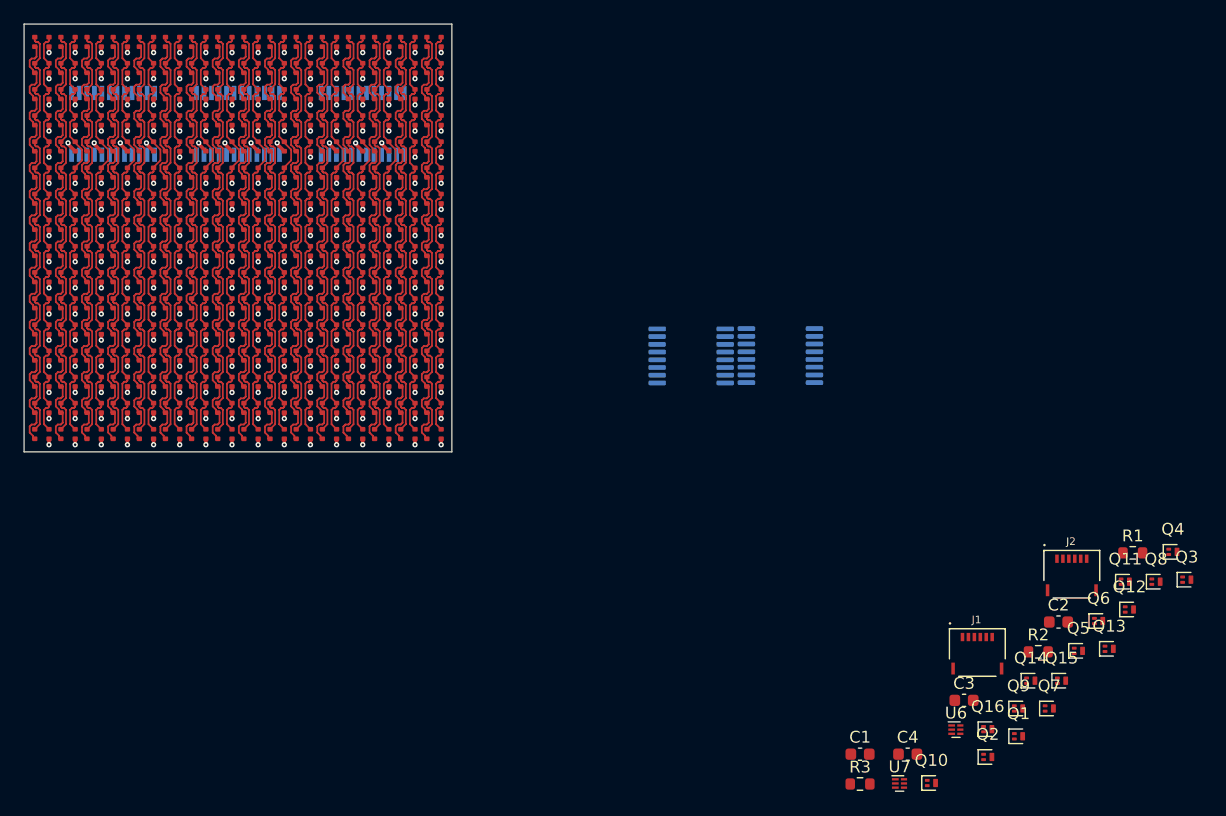
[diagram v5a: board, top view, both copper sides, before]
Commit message: Placed row driver MOSFETs
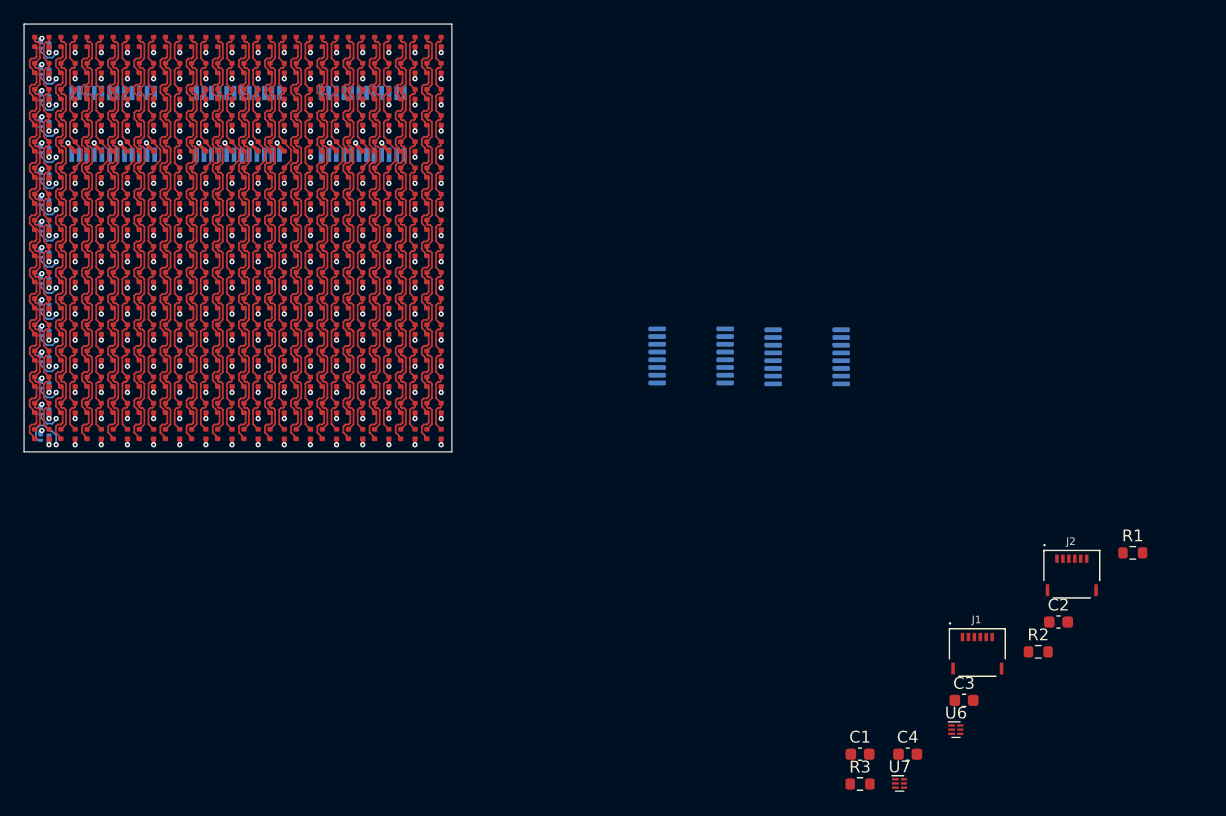
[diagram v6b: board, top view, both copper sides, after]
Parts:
- Q1, Q10, Q11, Q12, Q13, Q14, Q15, Q16, Q2, Q3, Q4, Q5, Q6, Q7, Q8, Q9: moved to B.Cu
- moved Q3 104.3 mm to (61.8, 66.2)
- moved Q4 101.5 mm to (61.8, 68.4)
- moved Q1 100.5 mm to (61.8, 61.8)
- moved Q8 98.1 mm to (61.8, 77.2)
- moved Q2 98.1 mm to (61.8, 64.0)
- moved Q5 96.6 mm to (61.8, 70.6)
- moved Q6 96.3 mm to (61.8, 72.8)
- moved Q7 94.7 mm to (61.8, 75.0)
- moved Q12 94.2 mm to (61.8, 86.0)
- moved Q11 93.8 mm to (61.8, 83.8)
- moved Q13 92.8 mm to (61.8, 88.2)
- moved Q9 90.4 mm to (61.8, 79.4)
- moved Q15 88.5 mm to (61.8, 92.6)
- moved Q14 86.6 mm to (61.8, 90.4)
- moved Q10 85.7 mm to (61.8, 81.6)
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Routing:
- net /ROW_15/COMMON: track 41.0 -> 50.0 mm
- net VCC: track 0.00 -> 5.46 mm, vias 0 -> 16
- net /ROW_15: track 0.00 -> 4.19 mm, vias 0 -> 1
- net /ROW_7: track 0.00 -> 2.03 mm, vias 0 -> 1
- net /ROW_6: track 0.00 -> 2.03 mm, vias 0 -> 1
- net /ROW_2: track 0.00 -> 2.03 mm, vias 0 -> 1
- net /ROW_12: track 0.00 -> 2.03 mm, vias 0 -> 1
- net /ROW_11: track 0.00 -> 2.03 mm, vias 0 -> 1
- net /ROW_1: track 0.00 -> 2.03 mm, vias 0 -> 1
- net /ROW_0: track 0.00 -> 2.03 mm, vias 0 -> 1
- net /ROW_8: track 0.00 -> 2.03 mm, vias 0 -> 1
- net /ROW_3: track 0.00 -> 2.03 mm, vias 0 -> 1
- net /ROW_13: track 0.00 -> 2.03 mm, vias 0 -> 1
- net /ROW_9: track 0.00 -> 2.03 mm, vias 0 -> 1
- net /ROW_5: track 0.00 -> 2.03 mm, vias 0 -> 1
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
